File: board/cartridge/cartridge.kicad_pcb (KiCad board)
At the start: 2 copper layers, 58.4 x 56 mm, 41 parts, among them J1 TF-115-BCP9, J2 KH-TYPE-C-16P, J3 TC2030-NL, P1 Card Edge, SW1 K3-1410S, SW2 K3-1410S, U1 STM32G0B0RETx, U2 NAU8814Y, U3 AMS1117-3.3, Y1 X322516MLB4SI

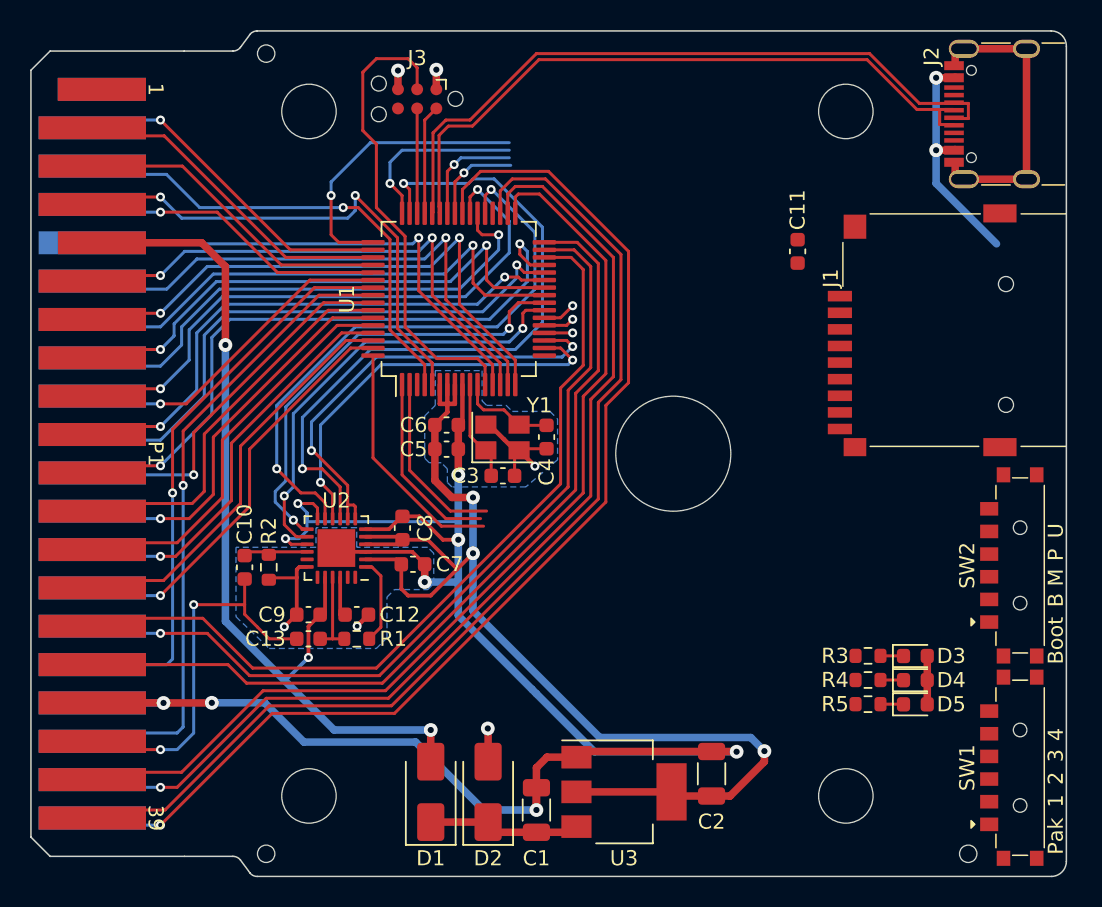
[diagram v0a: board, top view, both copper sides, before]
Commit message: Route everything else.
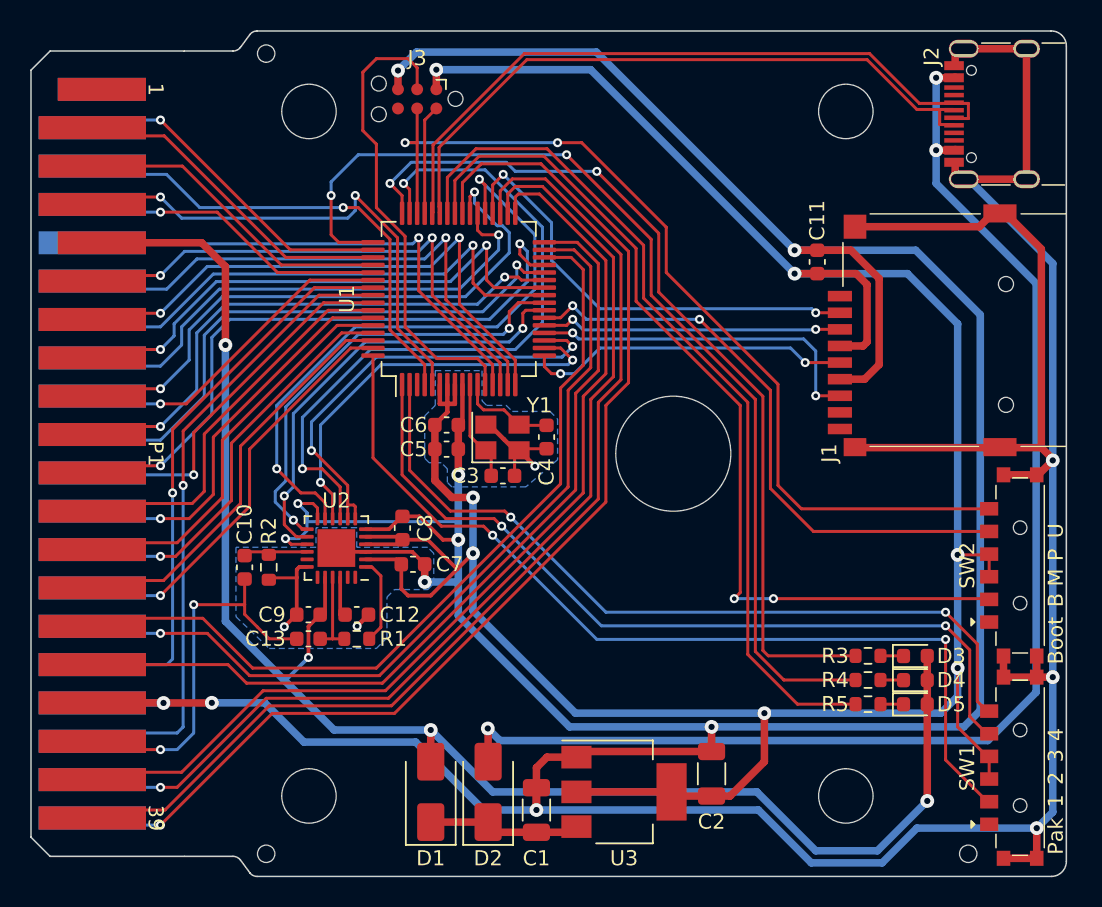
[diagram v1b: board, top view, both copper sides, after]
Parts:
- moved C11 1.48 mm to (163.5, 87.3)
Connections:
- J1 pad 9: /SD_DET -> unconnected-(J1-DET-Pad9)
- SW1 pad 7: (no net) -> GND
- SW2 pad 7: (no net) -> GND
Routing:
- net GND: track 165.0 -> 404.3 mm, vias 13 -> 17
- net +3V3: track 79.3 -> 182.9 mm, vias 4 -> 7
- net VBUS: track 17.4 -> 86.2 mm
- net /SWD_CLK: track 6.94 -> 62.2 mm, vias 0 -> 2
- net /BOOT_M: track 6.23 -> 60.5 mm, vias 1 -> 2
- net /LED_B: track 7.25 -> 57.3 mm, vias 1 -> 0
- net /LED_G: track 19.4 -> 68.3 mm, vias 1 -> 2
- net /LED_R: track 11.9 -> 59.4 mm, vias 1 -> 2
- net /PAK_2: track 16.0 -> 61.7 mm, vias 0 -> 2
- net +5V: track 62.4 -> 106.3 mm, vias 3 -> 4
- net /PAK_3: track 12.5 -> 54.7 mm, vias 0 -> 2
- net /PAK_4: track 12.1 -> 53.1 mm, vias 0 -> 2
- net /BOOT_P: track 2.21 -> 39.8 mm, vias 1 -> 2
- net /SD_~{CS}: track 0.00 -> 30.4 mm, vias 0 -> 2
- net /SD_SCLK: track 0.00 -> 21.6 mm, vias 0 -> 2
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
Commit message: Misc board cleanup.
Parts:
- added G1: LOGO, 0Project:Symbol_Bonsai_6.7mm, B.Cu at (169.0, 100.0)
- added G2: OSHW-Symbol_6.7x6mm_SilkScreen, Symbol:OSHW-Symbol_6.7x6mm_SilkScreen, B.Cu at (163.0, 100.0)
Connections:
- U1 pad 3: unconnected-(U1-PC13-Pad3) -> VBUS
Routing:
- net VBUS: track 86.2 -> 117.0 mm, vias 3 -> 5
- net +3V3: track 182.9 -> 183.7 mm
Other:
- board text added: "CoCo Chameleon ${REVISION}"
- board text added: "JLCJLCJLCJLC"
- board text added: "TRS-80 Color Computer Cartridge Emulator ${COMPANY} ${COMMENT1}"

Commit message: Final cleanup for first cartridge prototype.
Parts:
- J2: value KH-TYPE-C-16P -> HC-TYPE-C-16P-01B; footprint 0Project:KH-TYPE-C-16P -> 0Project:HC-TYPE-C-16P-01B
- R3: value 150R -> 220R
- R4: value 100R -> 120R
- R5: value 100R -> 150R
- moved J2 0.23 mm to (174.7, 77.5)
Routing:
- net VBUS: track 117.0 -> 117.9 mm

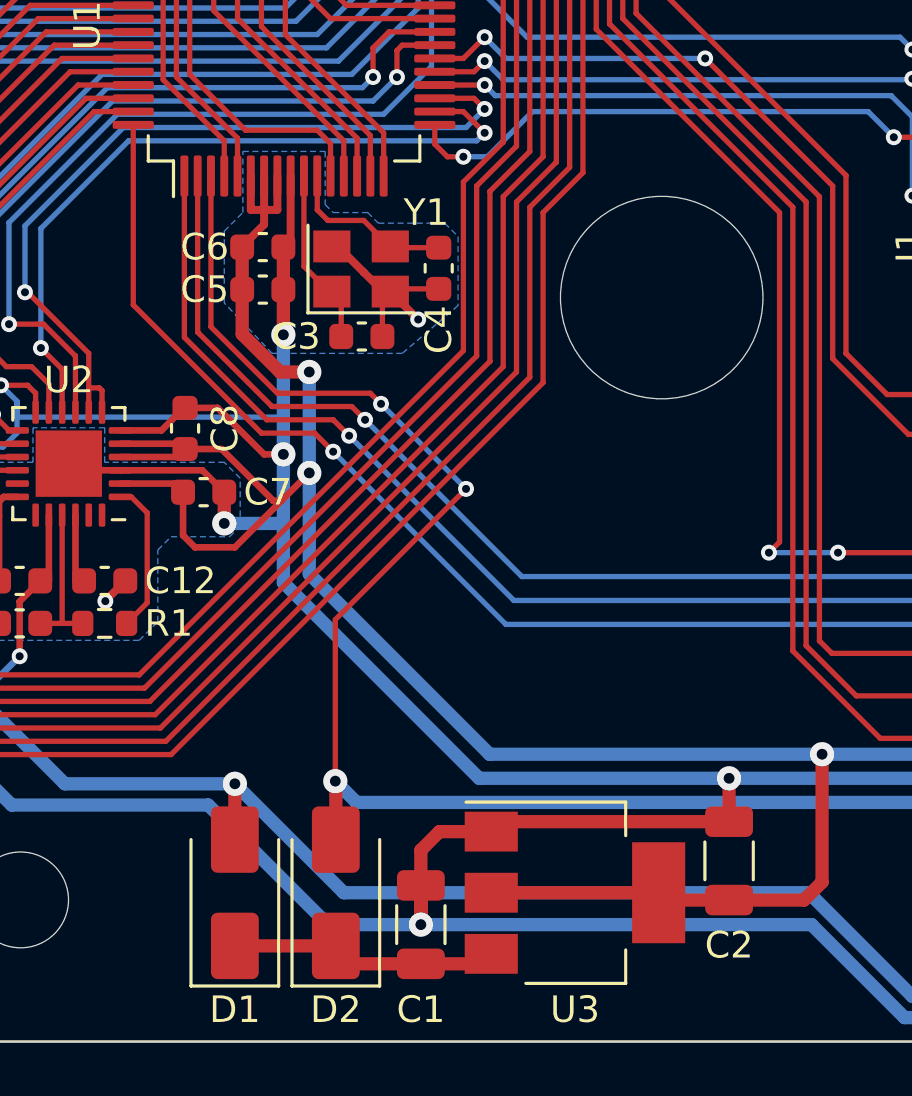
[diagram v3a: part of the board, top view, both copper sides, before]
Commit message: Update KiCad projects to v8.
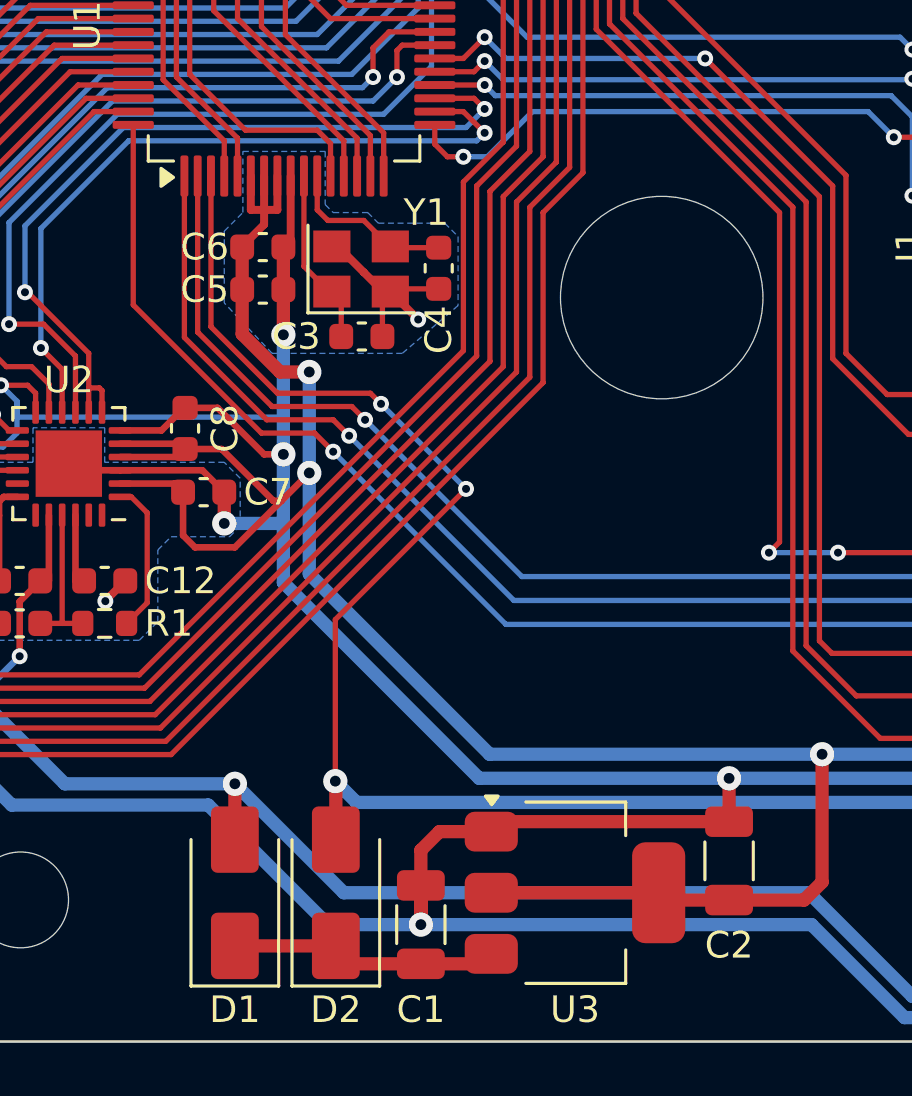
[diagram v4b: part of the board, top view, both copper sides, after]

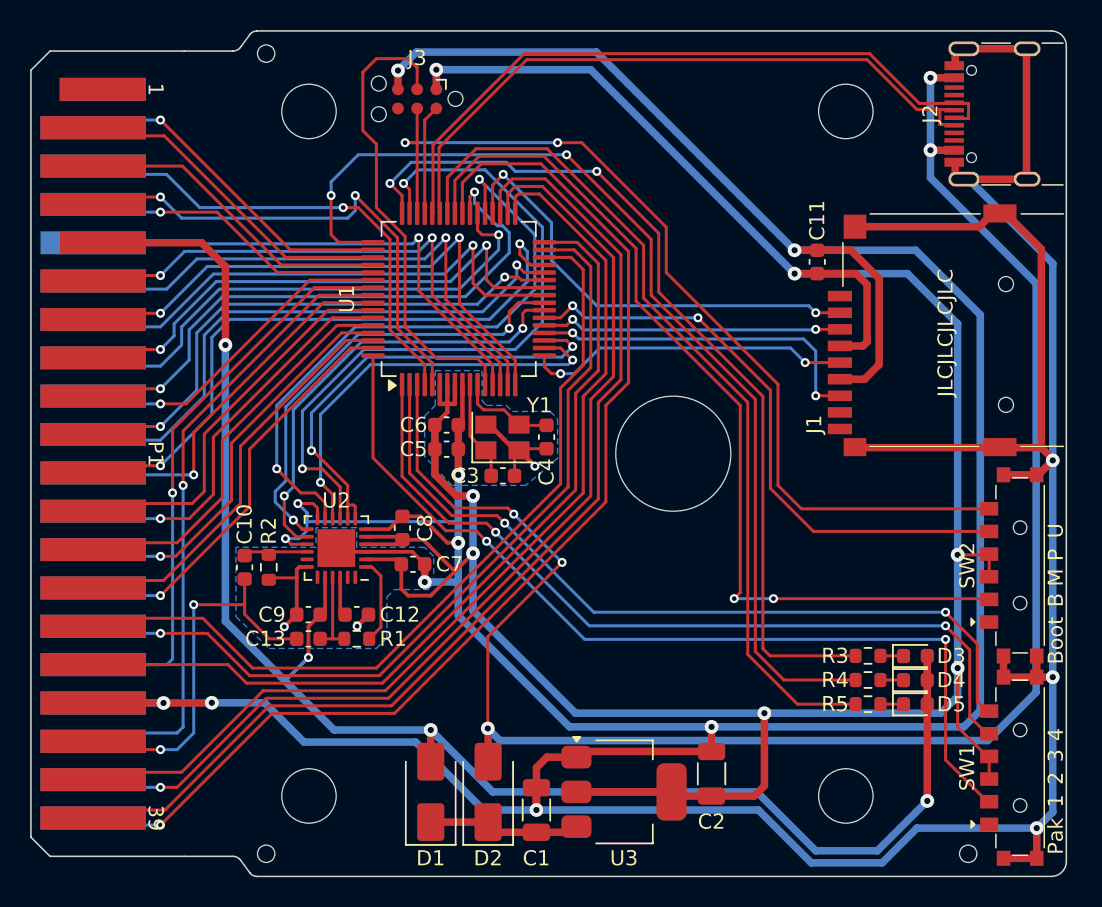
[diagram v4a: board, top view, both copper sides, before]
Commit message: Design and mostly route level shifters.
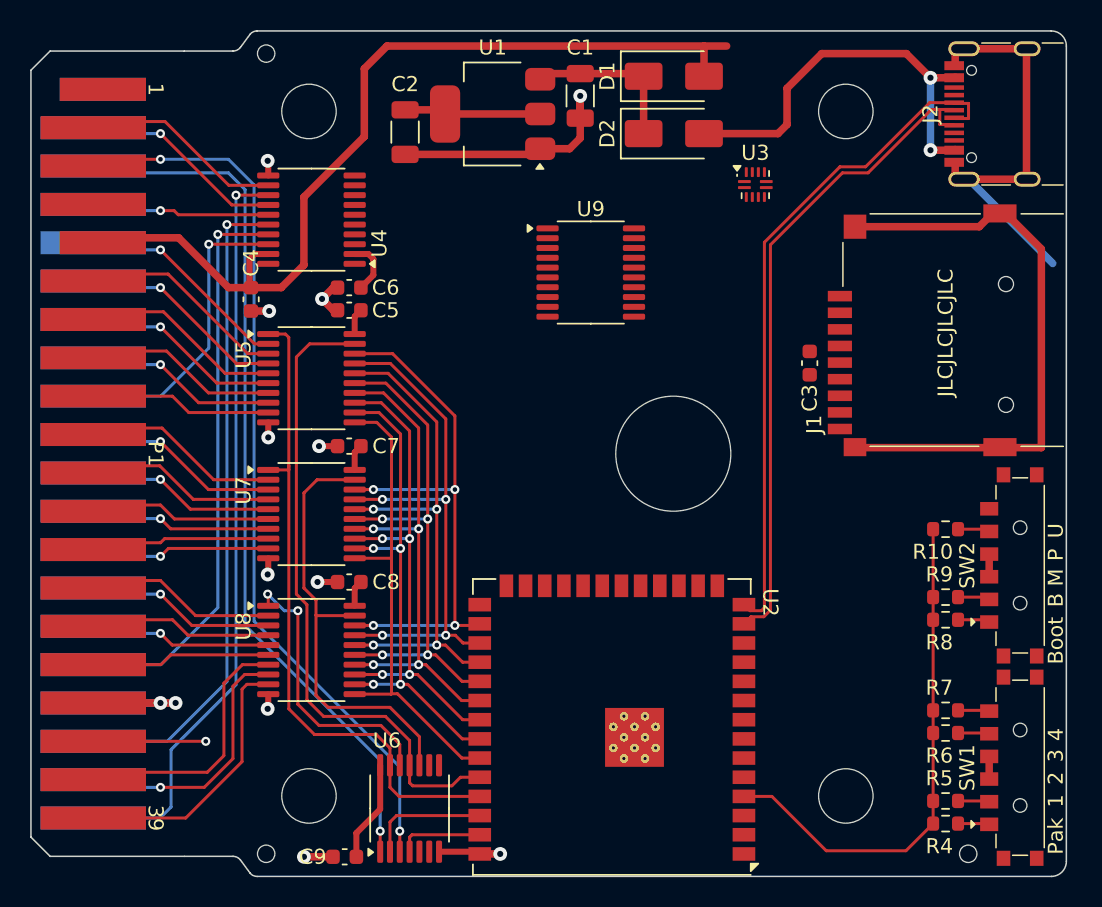
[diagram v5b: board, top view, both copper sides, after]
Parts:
- removed C10, C13: 1u, Capacitor_SMD:C_0603_1608Metric
- removed C12: 4u7, Capacitor_SMD:C_0603_1608Metric
- removed the C3 at (142.7, 101.5)
- removed D3: KT-0603R, LED_SMD:LED_0603_1608Metric
- removed D4: 19-217/GHC-YR1S2/3T, LED_SMD:LED_0603_1608Metric
- removed D5: 19-217/BHC-ZL1M2RY/3T, LED_SMD:LED_0603_1608Metric
- removed J3: TC2030-NL, Connector:Tag-Connect_TC2030-IDC-NL_2x03_P1.27mm_Vertical
- removed R1, R2: 100k, Resistor_SMD:R_0603_1608Metric
- removed R3: 220R, Resistor_SMD:R_0603_1608Metric
- removed the U1 at (139.8, 89.8)
- removed Y1: X322516MLB4SI, Crystal:Crystal_SMD_3225-4Pin_3.2x2.5mm
- added R10: 1k5 1%, Resistor_SMD:R_0603_1608Metric, F.Cu at (172.0, 105.0)
- added R6: 3k9 1%, Resistor_SMD:R_0603_1608Metric, F.Cu at (172.0, 118.5)
- added R7: 4k7 1%, Resistor_SMD:R_0603_1608Metric, F.Cu at (172.0, 117.0)
- added R8: 6k8 1%, Resistor_SMD:R_0603_1608Metric, F.Cu at (172.0, 111.0)
- added R9: 3k3 1%, Resistor_SMD:R_0603_1608Metric, F.Cu at (172.0, 109.5)
- added U3: TUSB320, Package_DFN_QFN:Texas_X2QFN-12_1.6x1.6mm_P0.4mm, F.Cu at (159.4, 82.2)
- added U4: TXS0108E, Package_SO:TSSOP-20_4.4x6.5mm_P0.65mm, F.Cu at (130.0, 84.5)
- added U5: 74LVC245, Package_SO:TSSOP-20_4.4x6.5mm_P0.65mm, F.Cu at (130.0, 95.0)
- added U6: 74LVT14, Package_SO:TSSOP-14_4.4x5mm_P0.65mm, F.Cu at (136.5, 123.5)
- added U7: 74LVC541, Package_SO:TSSOP-20_4.4x6.5mm_P0.65mm, F.Cu at (130.0, 104.0)
- added U8: 74LVC541, Package_SO:TSSOP-20_4.4x6.5mm_P0.65mm, F.Cu at (130.0, 113.0)
- added U9: PCM5100, Package_SO:TSSOP-20_4.4x6.5mm_P0.65mm, F.Cu at (148.5, 88.0)
- C4: value 18p -> 100n
- C5, C7, C8, C9: value 4u7 -> 100n
- R4: value 120R -> 2k7 1%
- R5: value 150R -> 3k3 1%
- U2: value NAU8814Y -> ESP32-S3-WROOM-1U; footprint Package_DFN_QFN:VQFN-24-1EP_4x4mm_P0.5mm_EP2.5x2.5mm -> RF_Module:ESP32-S3-WROOM-1U
- moved D1 50.1 mm to (154.0, 75.0), turned to 0 degrees
- moved C1 47.4 mm to (147.8, 76.3), turned to -90 degrees
- moved C2 47.1 mm to (136.2, 78.7), turned to -90 degrees
- moved U1 45.7 mm to (142.0, 77.5), turned to 180 degrees
- moved D2 45.3 mm to (154.0, 78.8), turned to 0 degrees
- moved U2 21.8 mm to (149.9, 118.1)
- moved C4 21.6 mm to (126.0, 89.8)
- moved C9 16.2 mm to (132.2, 126.7)
- moved C5 11.2 mm to (132.5, 90.5), turned to 180 degrees
- moved C6 11.2 mm to (132.5, 89.0), turned to 180 degrees
- moved R4 10.8 mm to (172.0, 124.5), turned to 180 degrees
- moved C7 8.89 mm to (132.5, 99.5), turned to 180 degrees
- moved R5 8.21 mm to (172.0, 123.0), turned to 180 degrees
- moved C3 6.72 mm to (163.0, 94.0), turned to -90 degrees
- moved C8 5.02 mm to (132.5, 108.5), turned to 180 degrees
- renumbered C11 to C3, U3 to U1
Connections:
- C4 pad 1: /OSC_OUT -> +5V
- C9 pad 1: +5V -> +3V3
- J1 pad 1: unconnected-(J1-DAT2-Pad1) -> /SD_DAT2
- J1 pad 2: /SD_~{CS} -> /SD_DAT3
- J1 pad 3: /SD_MOSI -> /SD_CMD
- J1 pad 5: /SD_SCLK -> /SD_CLK
- J1 pad 7: /SD_MISO -> /SD_DAT0
- J1 pad 8: unconnected-(J1-DAT1-Pad8) -> /SD_DAT1
- J2 pad A5: unconnected-(J2-CC1-PadA5) -> /USB_CC1
- J2 pad A7: /USB_DN -> /USB_DM
- J2 pad B5: unconnected-(J2-CC2-PadB5) -> /USB_CC2
- J2 pad B7: /USB_DN -> /USB_DM
- P1 pad 10: /D0 -> /Host/D0
- P1 pad 11: /D1 -> /Host/D1
- P1 pad 12: /D2 -> /Host/D2
- P1 pad 13: /D3 -> /Host/D3
- P1 pad 14: /D4 -> /Host/D4
- P1 pad 15: /D5 -> /Host/D5
- P1 pad 16: /D6 -> /Host/D6
- P1 pad 17: /D7 -> /Host/D7
- P1 pad 18: /R/~{W} -> /Host/R/~{W}
- P1 pad 19: /A0 -> /Host/A0
- P1 pad 20: /A1 -> /Host/A1
- P1 pad 21: /A2 -> /Host/A2
- P1 pad 22: /A3 -> /Host/A3
- P1 pad 23: /A4 -> /Host/A4
- P1 pad 24: /A5 -> /Host/A5
- P1 pad 25: /A6 -> /Host/A6
- P1 pad 26: /A7 -> /Host/A7
- P1 pad 27: /A8 -> /Host/A8
- P1 pad 28: /A9 -> /Host/A9
- P1 pad 29: /A10 -> /Host/A10
- P1 pad 3: /~{HALT} -> /Host/~{HALT}
- P1 pad 30: /A11 -> /Host/A11
- P1 pad 31: /A12 -> /Host/A12
- P1 pad 32: /~{CTS} -> /Host/~{CTS}
- P1 pad 35: /SND -> /Host/SND
- P1 pad 36: /~{SCS} -> /Host/~{SCS}
- P1 pad 37: /A13 -> /Host/A13
- P1 pad 38: /A14 -> /Host/A14
- P1 pad 39: /A15 -> /Host/A15
- P1 pad 4: /~{NMI} -> /Host/~{NMI}
- P1 pad 40: /~{SLENB} -> /Host/~{SLENB}
- P1 pad 5: /~{RESET} -> /Host/~{RESET}
- P1 pad 6: /E -> /Host/E
- P1 pad 7: /Q -> unconnected-(P1-Q-Pad7)
- P1 pad 8: /~{CART} -> /Host/~{CART}
- R4 pad 1: /LED_G -> Net-(R4-Pad1)
- R4 pad 2: Net-(D4-K) -> /SWITCHES
- R5 pad 1: /LED_B -> Net-(R5-Pad1)
- R5 pad 2: Net-(D5-K) -> /SWITCHES
- SW1 pad 1: unconnected-(SW1-Pad1) -> Net-(R4-Pad1)
- SW1 pad 2: /PAK_2 -> Net-(R5-Pad1)
- SW1 pad 5: /PAK_3 -> Net-(SW1-3)
- SW1 pad 6: /PAK_4 -> Net-(SW1-4)
- SW2 pad 1: unconnected-(SW2-Pad1) -> Net-(R8-Pad1)
- SW2 pad 2: /BOOT_M -> Net-(R9-Pad1)
- SW2 pad 3: +3V3 -> GND
- SW2 pad 4: +3V3 -> GND
- SW2 pad 5: /BOOT_P -> Net-(SW2-3)
- SW2 pad 6: /SWD_CLK -> /A/~{D}/~{DFU}
- U2 pad 1: Net-(U2-MICBIAS) -> GND
- U2 pad 10: /I2S_CK -> unconnected-(U2-GPIO17-Pad10)
- U2 pad 11: /I2S_MCK -> unconnected-(U2-GPIO18-Pad11)
- U2 pad 12: GND -> unconnected-(U2-GPIO8-Pad12)
- U2 pad 13: /I2C_SCL -> /USB_DM
- U2 pad 14: /I2C_SDA -> /USB_DP
- U2 pad 15: GND -> unconnected-(U2-GPIO3-Pad15)
- U2 pad 16: Net-(U2-MOUT) -> unconnected-(U2-GPIO46-Pad16)
- U2 pad 18: GND -> unconnected-(U2-GPIO10-Pad18)
- U2 pad 20: +5V -> unconnected-(U2-GPIO12-Pad20)
- U2 pad 21: Net-(U2-AUX) -> unconnected-(U2-GPIO13-Pad21)
- U2 pad 22: Net-(U2-VREF) -> unconnected-(U2-GPIO14-Pad22)
- U2 pad 24: unconnected-(U2-MIC+-Pad24) -> /IN_H/~{OUT_L}
- U2 pad 25: GND -> unconnected-(U2-GPIO48-Pad25)
- U2 pad 3: GND -> unconnected-(U2-EN-Pad3)
- U2 pad 4: +3V3 -> /SWITCHES
- U2 pad 5: +3V3 -> unconnected-(U2-GPIO5-Pad5)
- U2 pad 6: GND -> unconnected-(U2-GPIO6-Pad6)
- U2 pad 7: /I2S_SD -> unconnected-(U2-GPIO7-Pad7)
- U2 pad 8: /I2S_SD -> unconnected-(U2-GPIO15-Pad8)
- U2 pad 9: /I2S_WS -> unconnected-(U2-GPIO16-Pad9)
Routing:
- net GND: track 404.4 -> 112.6 mm, vias 17 -> 13
- net +3V3: track 183.7 -> 26.1 mm, vias 7 -> 0
- net VBUS: track 117.9 -> 27.4 mm, vias 5 -> 2
- net /~{SLENB}: track 76.2 -> 0.00 mm, vias 1 -> 0
- net /A15: track 71.0 -> 0.00 mm
- net /LED_G: track 68.3 -> 0.00 mm, vias 2 -> 0
- net /A14: track 68.1 -> 0.00 mm, vias 1 -> 0
- net /A13: track 65.4 -> 0.00 mm
- net /SWD_CLK: track 62.2 -> 0.00 mm, vias 2 -> 0
- net /PAK_2: track 61.7 -> 0.00 mm, vias 2 -> 0
- net /BOOT_M: track 60.5 -> 0.00 mm, vias 2 -> 0
- net /Host/~{RESET}: track 0.00 -> 59.7 mm, vias 0 -> 2
- net /LED_R: track 59.3 -> 0.00 mm, vias 2 -> 0
- net /Host/E: track 0.00 -> 58.3 mm, vias 0 -> 1
- net /A12: track 57.6 -> 0.00 mm
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- added copper zone on In1.Cu, net GND
- added copper zone on In2.Cu, net GND
- removed copper zone on B.Cu, net GND
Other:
- copper layers 2 -> 4
